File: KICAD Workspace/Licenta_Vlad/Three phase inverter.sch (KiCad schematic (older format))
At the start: 39 parts, among them U1 IR2101, U2 IR2101, U3 IR2101

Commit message: Added schematic for BEMF.
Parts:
- added 0.1uF1, C19, C20, C21, C22, C23, C? (x3): C_Small, symbol Device:C_Small
- added C13: CP1, symbol Device:CP1
- added C14, C15: 100uF, symbol Device:CP1
- added C16: 0.1uF, symbol Device:C
- added C17, C18: 330uF, symbol Device:CP1
- added C? (x2): 1, symbol Device:C_Small
- added D10: 1N5061, Diode_THT:D_DO-201AD_P15.24mm_Horizontal, symbol Diode:1N5400
- added D11, D12: 1N5828, Diode_THT:D_DO-201AD_P15.24mm_Horizontal, symbol Diode:1N5822
- added J? (x2): Conn_01x03, symbol Connector_Generic:Conn_01x03
- added J?: Conn_01x02, symbol Connector_Generic:Conn_01x02
- added L1, L2: 300uH, symbol pspice:INDUCTOR
- added R10, R11, R12, R13, R14, R15, R16, R17, R18, R19, R20, R21, R? (x6): R, symbol Device:R
- added U4: L7805, symbol Regulator_Linear:L7805
- added U5, U6: LM2574HVM-12, Package_SO:SOIC-14W_7.5x9.0mm_P1.27mm, symbol Regulator_Switching:LM2574HVM-12
- added U7: ACS754, Sensor_Current:Allegro_CB_PFF, symbol Sensor_Current:ACS756xCB-050B-PFF
- added U8, U9: LM393, symbol Comparator:LM393
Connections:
- net labels added: +5V, 12V, 12V_Board, 12V_Bootstrap, 5V, BEMF_A, BEMF_B, BEMF_C, BEMF_REF, CURRENT_SENSOR, EXTIA, EXTIB, EXTIC, V_BAT+, V_BAT-, V_BAT2+
- net labels removed: +BATT, 12V_IN, CP_OUT, Vbatt
- wire segments 170 -> 351
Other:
- note added: "12V Buck Converter 0.5A"
- note added: "12V Buck Converter 3A"
- note added: "5V output"
- note added: "SENSOR CURRENT"
- moved on the sheet: C1, C10, C11, C12, C2, C3, C4, C5, C6, C7, C8, C9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

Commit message: Added some footprints and some traces in PCB editor
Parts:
- removed U5, U6: LM2574HVM-12, Package_SO:SOIC-14W_7.5x9.0mm_P1.27mm, symbol Regulator_Switching:LM2574HVM-12
- added C29, C30: C_Small, Capacitor_THT:CP_Radial_D8.0mm_P3.50mm, symbol Device:C_Small
- added C31: C, Capacitor_THT:CP_Radial_D18.0mm_P7.50mm, symbol Device:C
- added D13: LED, LED_THT:LED_D5.0mm, symbol Device:LED
- added J4: Conn_01x02, Connector_PinHeader_2.54mm:PinHeader_1x02_P2.54mm_Vertical, symbol Connector_Generic:Conn_01x02
- added J5, J6: Conn_01x03, Connector_PinHeader_2.54mm:PinHeader_1x03_P2.54mm_Vertical, symbol Connector_Generic:Conn_01x03
- added Q1: BC547, Package_TO_SOT_THT:TO-92_Inline, symbol Transistor_BJT:BC547
- added Q2: IRF9530, Package_TO_SOT_THT:TO-220-3_Vertical, symbol Transistor_FET:IRF3205
- added R28: R, Resistor_THT:R_Axial_DIN0411_L9.9mm_D3.6mm_P15.24mm_Horizontal, symbol Device:R
- added R29, R30: 10K, Resistor_THT:R_Axial_DIN0411_L9.9mm_D3.6mm_P15.24mm_Horizontal, symbol Device:R
- added R31: 150K, Resistor_THT:R_Axial_DIN0411_L9.9mm_D3.6mm_P15.24mm_Horizontal, symbol Device:R
- added R32: 13K, Resistor_THT:R_Axial_DIN0411_L9.9mm_D3.6mm_P15.24mm_Horizontal, symbol Device:R
- added U10: LP2950-3.3_TO92, Package_TO_SOT_THT:TO-92_Inline, symbol Regulator_Linear:LP2950-3.3_TO92
- added U5, U6: LM2576HVT-12, Package_TO_SOT_THT:TO-220-5_Vertical, symbol Regulator_Switching:LM2576HVT-12
- 0.1uF1, C1, C10, C11, C12, C13, C14, C15, C16, C17, C18, C19, C2, C20, C21, C22, C23, C3, C4, C5, C6, C7, C8, C9: footprint (none) -> Capacitor_THT:CP_Radial_D8.0mm_P3.50mm
- C24, C25, C26, C27, C28: renamed from C?; footprint (none) -> Capacitor_THT:CP_Radial_D8.0mm_P3.50mm
- FQP85N1, FQP85N2, FQP85N3, FQP85N4, FQP85N5, FQP85N6: footprint (none) -> Package_TO_SOT_THT:FQP85N06
- J1: renamed from J?; footprint (none) -> Connector:MOTOR_CONNECTOR
- J2: renamed from J?; footprint (none) -> Battery:XT60
- J3: renamed from J?; footprint (none) -> Connector_PinHeader_2.54mm:PinHeader_1x03_P2.54mm_Vertical
- L1, L2: footprint (none) -> Inductor_THT:L_Axial_L7.0mm_D3.3mm_P5.08mm_Vertical_Fastron_MICC
- R1, R10, R11, R12, R13, R14, R15, R16, R17, R18, R19, R2, R20, R21, R3, R4, R5, R6, R7, R8, R9: footprint (none) -> Resistor_THT:R_Axial_DIN0411_L9.9mm_D3.6mm_P15.24mm_Horizontal
- R22, R23, R24, R25, R26, R27: renamed from R?; footprint (none) -> Resistor_THT:R_Axial_DIN0411_L9.9mm_D3.6mm_P15.24mm_Horizontal
- U1, U2, U3: footprint (none) -> IR2101:DIL08
- U4: footprint (none) -> Package_TO_SOT_THT:TO-220-3_Vertical
- U8, U9: footprint (none) -> LM393AN:DIP254P762X508-8
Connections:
- net 12V is gone; now on net 12V_Bootstrap: C13.1, U4.1 (IN)
- net 12V_Board: now also J4.1 (Pin_1), U5.4 (FB)
- net 12V_Bootstrap: now also U6.4 (FB)
- net 5V: now also C29.1, U10.3 (VI)
- net GNDREF: now also C29.2, C30.2, C31.2, D13.1 (K), J4.2 (Pin_2), Q1.3 (E), R32.2, U10.2 (GND), U5.3 (GND), U5.5 (~ON~/OFF), U6.3 (GND), U6.5 (~ON~/OFF)
- net V_BAT+: now also C31.1; no longer FQP85N1.1 (D), FQP85N3.1 (D), FQP85N5.1 (D)
- net V_BAT2+: now also FQP85N1.1 (D), FQP85N3.1 (D), FQP85N5.1 (D), Q2.2 (D), R30.1, U5.1 (VIN), U6.1 (VIN)
- net at D11.1 (K), L1.1: now also U5.2 (OUT)
- net at D12.1 (K), L2.1: now also U6.2 (OUT)
- net HIN_1 renamed HIN1
- net HIN1: now also J5.1 (Pin_1)
- net HIN_2 renamed HIN2
- net HIN2: now also J5.2 (Pin_2)
- net HIN_3 renamed HIN3
- net HIN3: now also J5.3 (Pin_3)
- net LIN_1 renamed LIN1
- net LIN1: now also J6.1 (Pin_1)
- net LIN_2 renamed LIN2
- net LIN2: now also J6.2 (Pin_2)
- net LIN_3 renamed LIN3
- net LIN3: now also J6.3 (Pin_3)
- new net: Q1.2 (B), R29.1
- new net: Q1.1 (C), Q2.1 (G), R30.2
- new net: Q2.3 (S), R31.1
- new net: C30.1, R28.1, U10.1 (VO)
- new net: D13.2 (A), R28.2
- new net BATT_VOLTAGE: R31.2, R32.1
- new net READ_CMD: R29.2

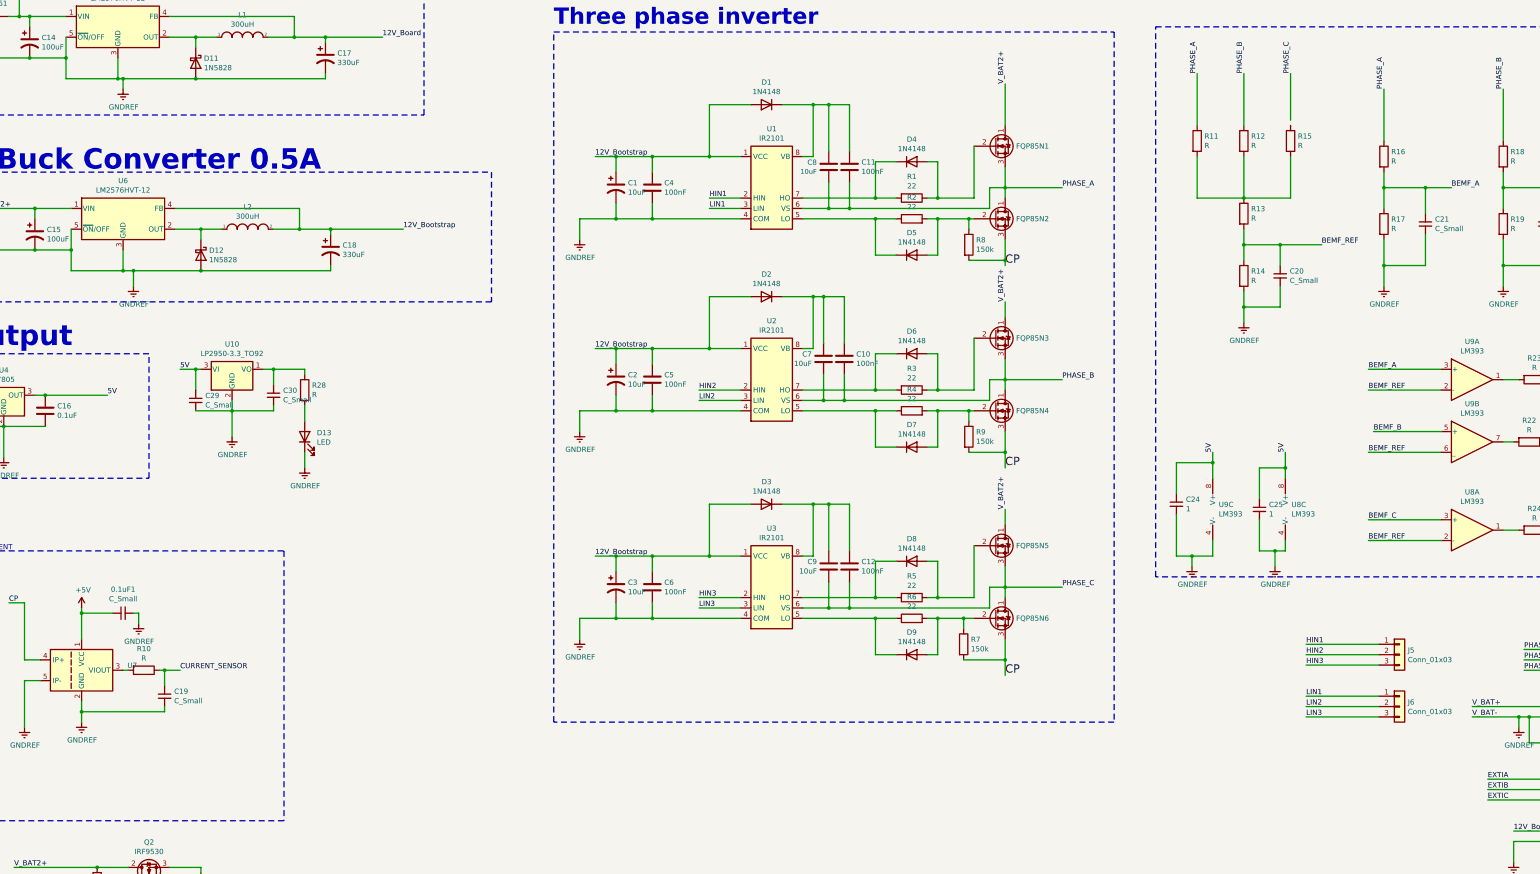
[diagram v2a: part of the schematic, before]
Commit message: PCB version 1 after big big failure .......................
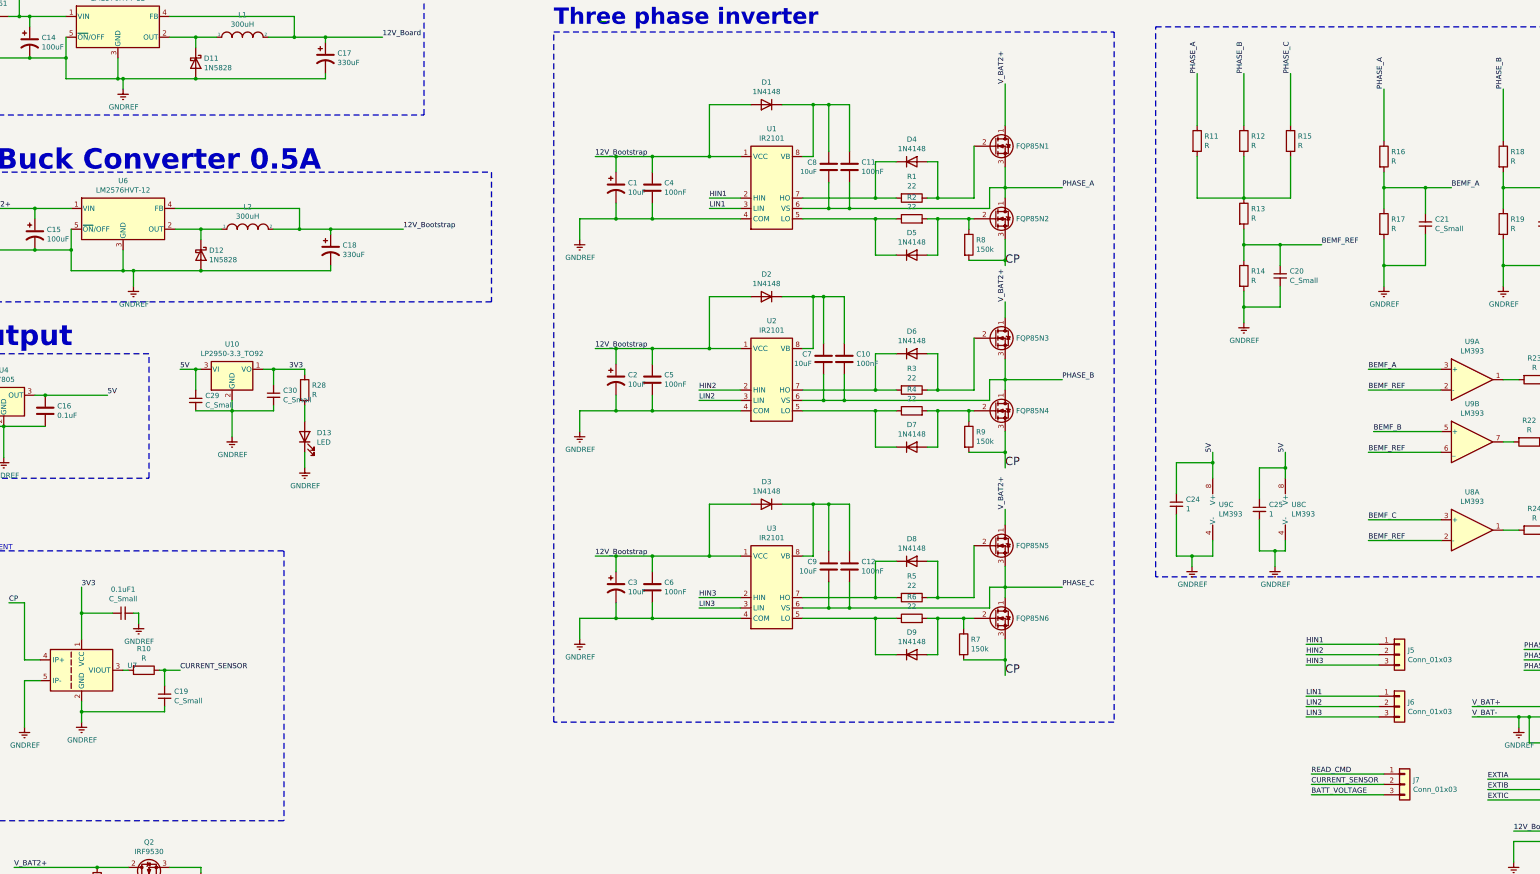
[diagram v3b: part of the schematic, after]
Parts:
- added J7: Conn_01x03, Connector_PinHeader_2.54mm:PinHeader_1x03_P2.54mm_Vertical, symbol Connector_Generic:Conn_01x03
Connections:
- net +5V is gone; now on net 3V3: 0.1uF1.1, U7.1 (VCC)
- net BATT_VOLTAGE: now also J7.3 (Pin_3)
- net CURRENT_SENSOR: now also J7.2 (Pin_2)
- net PHASE_C: now also R15.1
- net READ_CMD: now also J7.1 (Pin_1)
- net 3V3: now reaches C30.1, R28.1, U10.1 (VO)
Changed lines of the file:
@@
 PHASE_A
-Wire Wire Line
-	14350 2550 14350 2100
 Wire Wire Line
 	13900 2600 13900 2100
@@
 Wire Wire Line
 	2700 7300 3000 7300
-Wire Wire Line
-	2700 7300 2700 7250
 Connection ~ 2700 7300
 Wire Wire Line
@@
 Wire Wire Line
 	2300 7750 2150 7750
-$Comp
-L power:+5V #PWR?
-U 1 1 5CC2E1EC
-P 2700 7250
-AR Path="/5CC2E1EC" Ref="#PWR?"  Part="1"
-AR Path="/5CB87033/5CC2E1EC" Ref="#PWR?"  Part="1"
-AR Path="/5CB00088/5CC2E1EC" Ref="#PWR07"  Part="1"
-F 0 "#PWR07" H 2700 7100 50  0001 C CNN
-F 1 "+5V" H 2715 7423 50  0000 C CNN
-F 2 "" H 2700 7250 50  0001 C CNN
-F 3 "" H 2700 7250 50  0001 C CNN
-	1    2700 7250
-	1    0    0    -1
-$EndComp
 Connection ~ 2700 8250
 Wire Wire Line
@@
 	0    1    1    0
 $EndComp
+$Comp
+L Connector_Generic:Conn_01x03 J7
+U 1 1 5CA30E81
+P 15450 8950
+F 0 "J7" H 15530 8992 50  0000 L CNN
+F 1 "Conn_01x03" H 15530 8901 50  0000 L CNN
+F 2 "Connector_PinHeader_2.54mm:PinHeader_1x03_P2.54mm_Vertical" H 15450 8950 50  0001 C CNN
+F 3 "~" H 15450 8950 50  0001 C CNN
+	1    15450 8950
+	1    0    0    -1
+$EndComp
+Wire Wire Line
+	15250 8850 14550 8850
+Wire Wire Line
+	15250 8950 14550 8950
+Wire Wire Line
+	15250 9050 14550 9050
+Text Label 14550 8850 0    50   ~ 0
+READ_CMD
+Text Label 14550 8950 0    50   ~ 0
+CURRENT_SENSOR
+Text Label 14550 9050 0    50   ~ 0
+BATT_VOLTAGE
+Wire Wire Line
+	14350 2100 14350 2600
+Wire Wire Line
+	2700 7050 2700 7300
+Text Label 4700 4950 0    50   ~ 0
+3V3
+Text Label 2700 7050 0    50   ~ 0
+3V3
 $EndSCHEMATC

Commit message: Added inverter (only) pcb.
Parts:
- removed C14, C15: 100uF, Capacitor_THT:CP_Radial_D8.0mm_P3.50mm, symbol Device:CP1
- removed C17, C18: 330uF, Capacitor_THT:CP_Radial_D8.0mm_P3.50mm, symbol Device:CP1
- removed D10: 1N5061, Diode_THT:D_DO-201AD_P15.24mm_Horizontal, symbol Diode:1N5400
- removed D11, D12: 1N5828, Diode_THT:D_DO-201AD_P15.24mm_Horizontal, symbol Diode:1N5822
- removed J4: Conn_01x02, Connector_PinHeader_2.54mm:PinHeader_1x02_P2.54mm_Vertical, symbol Connector_Generic:Conn_01x02
- removed L1, L2: 300uH, Inductor_THT:L_Axial_L7.0mm_D3.3mm_P5.08mm_Vertical_Fastron_MICC, symbol pspice:INDUCTOR
- removed U5, U6: LM2576HVT-12, Package_TO_SOT_THT:TO-220-5_Vertical, symbol Regulator_Switching:LM2576HVT-12
- added J7: Conn_01x02, Connector_PinSocket_2.54mm:PinSocket_1x02_P2.54mm_Vertical, symbol Connector_Generic:Conn_01x02
- renumbered C13 to C1, C5 to C10, C6 to C11, C7 to C12, C8 to C13, C9 to C14, C10 to C15, C11 to C16, C12 to C17, C24 to C18, C25 to C19, C16 to C2, C26 to C23, C27 to C24, C28 to C25, C31 to C26, C23 to C27, C19 to C3, C29 to C4, C30 to C5, C1 to C6, C2 to C7, C3 to C8, C4 to C9, D13 to D1, D9 to D10, D1 to D2, D2 to D3, D3 to D4, D4 to D5, D5 to D6, D6 to D7, D7 to D8, D8 to D9, J5 to J1, J6 to J2, J7 to J3, J1 to J4, J2 to J5, J3 to J6, R29 to R1, R4 to R10, R5 to R11, R6 to R12, R7 to R13, R8 to R14, R9 to R15, R11 to R16, R12 to R17, R13 to R18, R14 to R19, R30 to R2, R15 to R20, R16 to R21, R17 to R22, R18 to R23, R19 to R24, R22 to R25, R23 to R26, R24 to R27, R25 to R28, R26 to R29, R10 to R3, R27 to R30, R20 to R31, R21 to R32, R31 to R4, R32 to R5, R28 to R6, R1 to R7, R2 to R8, R3 to R9, U4 to U1, U7 to U2, U10 to U3, U1 to U4, U2 to U5, U3 to U6, U9 to U7
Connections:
- net 12V_Bootstrap: now also J7.1 (Pin_1)
- net CP: now also U2.5 (IP-); no longer U2.4 (IP+)
- net GNDREF: now also U2.4 (IP+), J7.2 (Pin_2); no longer U2.5 (IP-)
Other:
- note removed: "12V Buck Converter 0.5A"
- note removed: "12V Buck Converter 3A"
- moved on the sheet: 0.1uF1, C1, C10, C11, C12, C13, C14, C15, C16, C17, C18, C19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

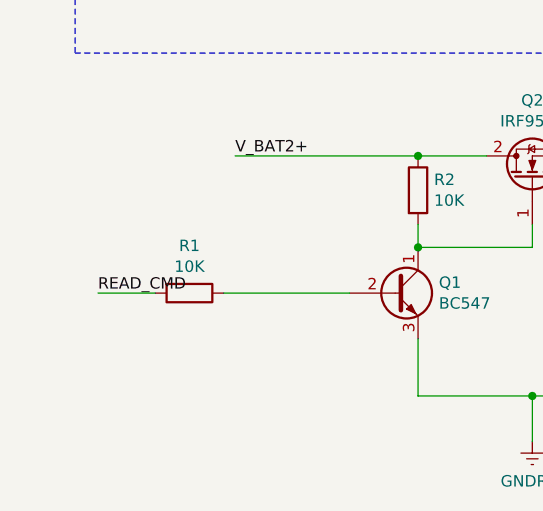
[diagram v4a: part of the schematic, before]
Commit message: SMD version
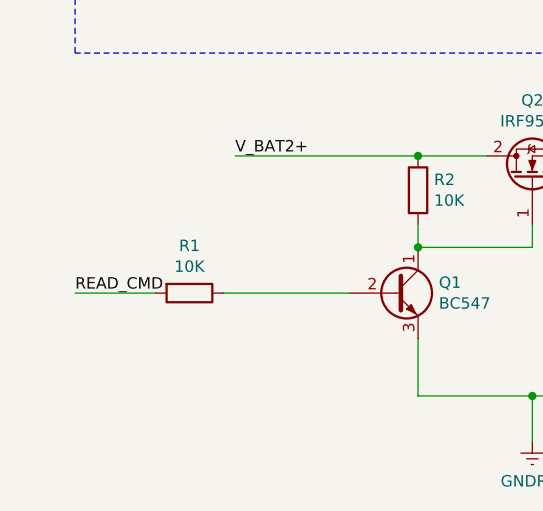
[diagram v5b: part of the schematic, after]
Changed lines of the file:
@@
 Text Label 8050 3100 0    50   ~ 0
 HIN1
-Text Label 1950 9950 0    50   ~ 0
+Text Label 1850 9950 0    50   ~ 0
 READ_CMD
-Wire Wire Line
-	2200 9950 1950 9950
 Text Label 5050 9800 0    50   ~ 0
 BATT_VOLTAGE
@@
 Text Label 15600 9350 0    50   ~ 0
 12V_Bootstrap
+Wire Wire Line
+	1850 9950 2200 9950
 $EndSCHEMATC
